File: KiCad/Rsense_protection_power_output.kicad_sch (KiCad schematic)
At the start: 62 parts, among them IC21 SN74LVC2G08DCTR, IC22 LM293D, IC23 OPA376AIDBVR, IC24 SN74LVC1G3157DCKR, IC25 SN74LVC1G3157DCKR, J1 572-0500, J2 572-0100, K1 FTR-C1GA012G-B05 or EE2-12NU-L, Q20 MMBT5551, Q21 MMBT5551, Q22 MMBT5551, Q23 MMBT5401, Q24 2N7002, X4 TBP03R1-350-03BE, X5 ZL263-20DG

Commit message: #5
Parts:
- R119: DigiKey 311-470CRCT-ND -> A129743CT-ND; Mouser 71-CRCW0805470RFKEB -> 652-CR0805FX-3300ELF; TME RC0805FR-07470R -> 0805S8F3300T5E
- R121: DigiKey (none) -> RC0805FR-071KL; Mouser (none) -> 603-RC0805FR-071KL; TME (none) -> RC0805FR-071K
- R144: DigiKey 311-470CRCT-ND -> RMCF0805FT220RCT-ND; Mouser 71-CRCW0805470RFKEB -> 603-RC0805FR-13220RL; TME RC0805FR-07470R -> 0805S8F2200T5E
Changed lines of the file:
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@@
 	(title_block
 		(title "${project_name}")
-		(date "2026-03-22")
+		(date "2026-03-23")
 		(rev "${project_version}")
 		(company "${project_creator}")
@@
 			)
 		)
-		(property "DigiKey" ""
+		(property "DigiKey" "RC0805FR-071KL"
 			(at 254 129.54 0)
 			(effects
@@
 			)
 		)
-		(property "Mouser" ""
+		(property "Mouser" "603-RC0805FR-071KL"
 			(at 254 129.54 0)
 			(effects
@@
 			)
 		)
-		(property "TME" ""
+		(property "TME" "RC0805FR-071K"
 			(at 254 129.54 0)
 			(effects
@@
 			)
 		)
-		(property "DigiKey" "311-470CRCT-ND"
+		(property "DigiKey" "RMCF0805FT220RCT-ND"
 			(at 200.66 134.62 0)
 			(effects
@@
 			)
 		)
-		(property "Mouser" "71-CRCW0805470RFKEB"
+		(property "Mouser" "603-RC0805FR-13220RL"
 			(at 200.66 134.62 0)
 			(effects
@@
 			)
 		)
-		(property "TME" "RC0805FR-07470R"
+		(property "TME" "0805S8F2200T5E"
 			(at 200.66 134.62 0)
 			(effects
@@
 			)
 		)
-		(property "DigiKey" "311-470CRCT-ND"
+		(property "DigiKey" "A129743CT-ND"
 			(at 195.58 129.54 0)
 			(effects
@@
 			)
 		)
-		(property "Mouser" "71-CRCW0805470RFKEB"
+		(property "Mouser" "652-CR0805FX-3300ELF"
 			(at 195.58 129.54 0)
 			(effects
@@
 			)
 		)
-		(property "TME" "RC0805FR-07470R"
+		(property "TME" "0805S8F3300T5E"
 			(at 195.58 129.54 0)
 			(effects

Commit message: #6
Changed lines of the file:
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@@
 	(title_block
 		(title "${project_name}")
-		(date "2026-03-23")
+		(date "2026-03-27")
 		(rev "${project_version}")
 		(company "${project_creator}")
@@
 		(dnp no)
 		(property "Reference" "C119"
-			(at 155.575 52.705 0)
+			(at 156.845 55.245 0)
 			(effects
 				(font

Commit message: #7
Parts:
- added R147, R148, R149, R150: 0R, PCM_EEZ_passives:R_0603_1608Metric, symbol PCM_EEZ_passives:R-EU
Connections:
- net I_SET: now also R147.2
- net I_SET_OUT: now also R147.1
- net POST_OUT+: now also R149.1
- net POST_OUT-: now also R150.2
- net SENSE+: now also R149.2
- net SENSE-: now also R150.1
- net U_SET: now also R148.2
- net U_SET_OUT: now also R148.1

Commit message: BOM and Gerbers update
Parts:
- C111: LCSC (none) -> C307541; TME (none) -> CL21B222JBANNNC
- D20, D21: LCSC (none) -> C109218
- R116, R117: LCSC (none) -> C60816
- R118: DigiKey (none) -> 13-RC0805FR-131RLCT-ND; LCSC (none) -> C7336808; Mouser (none) -> 603-RC0805FR-131RL; TME - -> RC0805FR-131RL
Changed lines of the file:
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@@
 			)
 		)
-		(property "LCSC" ""
+		(property "LCSC" "C60816"
 			(at 139.7 129.54 0)
 			(hide yes)
@@
 			)
 		)
-		(property "LCSC" ""
+		(property "LCSC" "C109218"
 			(at 116.84 154.94 0)
 			(hide yes)
@@
 						(name "Basic")
 						(dnp yes)
+						(in_bom no)
 					)
 				)
@@
 			)
 		)
-		(property "DigiKey" ""
+		(property "DigiKey" "13-RC0805FR-131RLCT-ND"
 			(at 149.86 55.88 0)
 			(hide yes)
@@
 			)
 		)
-		(property "LCSC" ""
+		(property "LCSC" "C7336808"
 			(at 149.86 55.88 0)
 			(hide yes)
@@
 			)
 		)
-		(property "Mouser" ""
+		(property "Mouser" "603-RC0805FR-131RL"
 			(at 149.86 55.88 0)
 			(hide yes)
@@
 			)
 		)
-		(property "TME" "-"
+		(property "TME" "RC0805FR-131RL"
 			(at 149.86 55.88 0)
 			(hide yes)
@@
 			)
 		)
-		(property "LCSC" ""
+		(property "LCSC" "C109218"
 			(at 233.68 124.46 0)
 			(hide yes)
@@
 						(name "Basic")
 						(dnp yes)
+						(in_bom no)
 					)
 				)
@@
 			)
 		)
-		(property "TME" ""
+		(property "TME" "CL21B222JBANNNC"
 			(at 68.58 40.64 0)
 			(hide yes)
@@
 			)
 		)
-		(property "LCSC" ""
+		(property "LCSC" "C307541"
 			(at 68.58 40.64 0)
 			(hide yes)
@@
 			)
 		)
-		(property "LCSC" ""
+		(property "LCSC" "C60816"
 			(at 142.24 129.54 0)
 			(hide yes)

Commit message: #8, schematics annotated
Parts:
- renumbered LED2 to LED3, Q20 to Q18, Q21 to Q19, Q22 to Q20, Q23 to Q21, Q24 to Q22, R99 to R102, R100 to R103, R101 to R104, R102 to R105, R103 to R106, R104 to R107, R105 to R108, R106 to R109, R107 to R110, R108 to R111, R109 to R112, R110 to R113, R111 to R114, R112 to R115, R113 to R116, R114 to R117, R149 to R118, R150 to R119, R148 to R120, R147 to R121, R115 to R122, R116 to R123, R117 to R124, R118 to R125, R119 to R126, R144 to R127, R120 to R128, R121 to R129, TP13 to TP14, TP14 to TP15

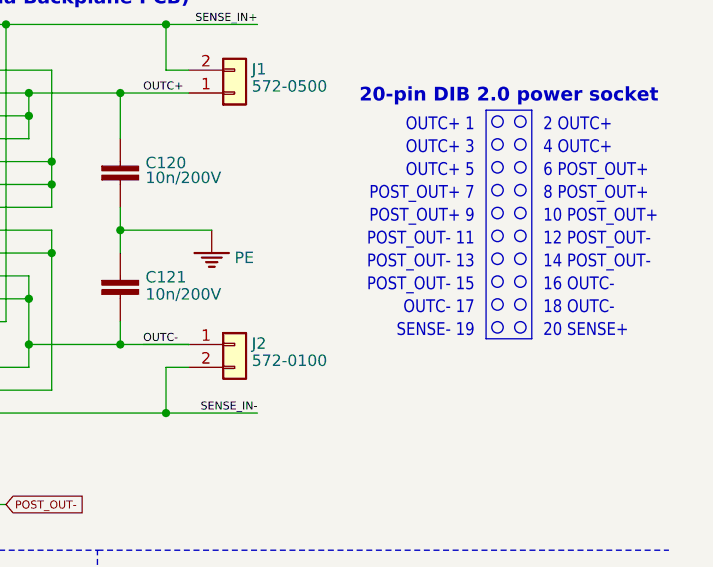
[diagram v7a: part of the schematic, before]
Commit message: Schematics update (power socket pinout)
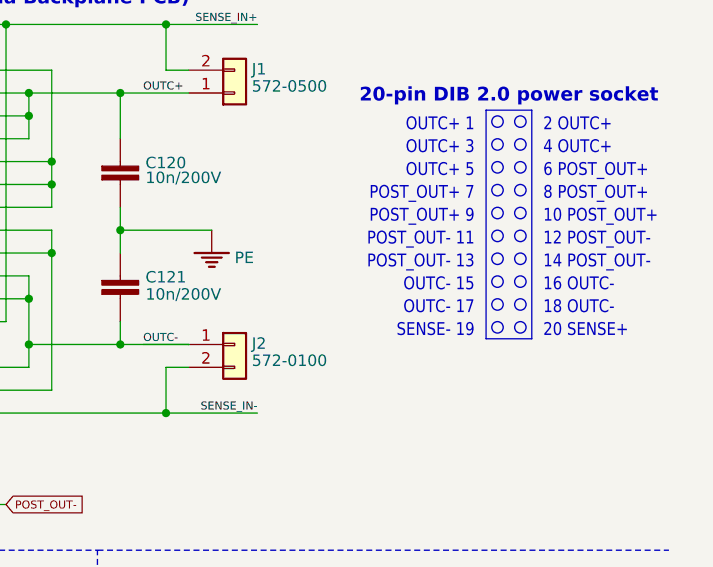
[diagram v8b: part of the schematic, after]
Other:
- note added: "OUTC- 15"
- note removed: "POST_OUT- 15"
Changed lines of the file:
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@@
 	(title_block
 		(title "${project_name}")
-		(date "2026-06-26")
+		(date "2026-06-30")
 		(rev "${project_version}")
 		(company "${project_creator}")
@@
 		)
 	)
-	(text "POST_OUT- 15"
+	(text "OUTC- 15"
 		(exclude_from_sim no)
 		(at 260.35 70.485 0)
